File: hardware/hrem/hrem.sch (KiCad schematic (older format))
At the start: 27 parts, among them J1 AVR-ISP, J2 Hall_Conn, Q1 MMBT4401-7-F, SW1 SW_Push_Dual, U1 HT7733A, U2 ATtiny85, U3 74LVC1G125, U4 74LVC1G125

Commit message: Button footprint added
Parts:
- SW1: footprint Button_Switch_SMD:SW_Push_1P1T_NO_6x6mm_H9.5mm -> hrem:Diptronics DTSM-65N
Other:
- moved on the sheet: TP1
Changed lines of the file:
@@
-$EndComp
-$Comp
-L Device:Battery_Cell BT1
-U 1 1 5D9F4947
-P 1850 1900
-F 0 "BT1" H 1968 1996 50  0000 L CNN
-F 1 "1xAAA" H 1968 1905 50  0000 L CNN
-F 2 "hrem:AAA battery" V 1850 1960 50  0001 C CNN
-F 3 "~" V 1850 1960 50  0001 C CNN
-	1    1850 1900
-	1    0    0    -1
 $EndComp
 $Comp
@@
 	2600 1600 2700 1600
 Wire Wire Line
-	1850 2000 1850 2050
-Wire Wire Line
-	1850 2050 2200 2050
-Wire Wire Line
 	2600 2050 2600 2000
 Wire Wire Line
 	2200 2100 2200 2050
-Connection ~ 2200 2050
 Wire Wire Line
 	2200 2050 2600 2050
@@
 F 0 "SW1" V 7600 1348 50  0000 L CNN
 F 1 "SW_Push_Dual" V 7645 1348 50  0001 L CNN
-F 2 "Button_Switch_SMD:SW_Push_1P1T_NO_6x6mm_H9.5mm" H 7600 1400 50  0001 C CNN
+F 2 "hrem:Diptronics DTSM-65N" H 7600 1400 50  0001 C CNN
 F 3 "https://datasheet.lcsc.com/szlcsc/Diptronics-DTSM-65N-V-T-R_C224982.pdf" H 7600 1400 50  0001 C CNN
 F 4 "C224982" H 7600 1200 50  0001 C CNN "Part"
@@
 $EndComp
 $Comp
-L Connector:TestPoint_Flag TP1
-U 1 1 5E2E9580
-P 1950 2900
-F 0 "TP1" H 2210 2948 50  0000 L CNN
-F 1 "TestPoint_Flag" H 2210 2903 50  0001 L CNN
-F 2 "TestPoint:TestPoint_Loop_D2.50mm_Drill1.0mm" H 2150 2900 50  0001 C CNN
-F 3 "~" H 2150 2900 50  0001 C CNN
-	1    1950 2900
-	1    0    0    -1
-$EndComp
-$Comp
-L power:GND #PWR02
-U 1 1 5E2ED3E9
-P 1950 3000
-F 0 "#PWR02" H 1950 2750 50  0001 C CNN
-F 1 "GND" H 1955 2827 50  0000 C CNN
-F 2 "" H 1950 3000 50  0001 C CNN
-F 3 "" H 1950 3000 50  0001 C CNN
-	1    1950 3000
-	1    0    0    -1
-$EndComp
-Wire Wire Line
-	1950 2900 1950 3000
-$Comp
 L Connector:TestPoint_Flag TP2
 U 1 1 5E2F0DC2
@@
 Wire Wire Line
 	9400 4750 9400 4850
+Connection ~ 2200 2050
+Wire Wire Line
+	2050 2050 2200 2050
+Connection ~ 2050 2050
+$Comp
+L Connector:TestPoint_Flag TP1
+U 1 1 5E2E9580
+P 2050 2050
+F 0 "TP1" H 2300 2250 50  0000 R CNN
+F 1 "TestPoint_Flag" H 2310 2053 50  0001 L CNN
+F 2 "TestPoint:TestPoint_Loop_D2.50mm_Drill1.0mm" H 2250 2050 50  0001 C CNN
+F 3 "~" H 2250 2050 50  0001 C CNN
+	1    2050 2050
+	-1   0    0    1
+$EndComp
+Wire Wire Line
+	1850 2050 2050 2050
+Wire Wire Line
+	1850 2000 1850 2050
+$Comp
+L Device:Battery_Cell BT1
+U 1 1 5D9F4947
+P 1850 1900
+F 0 "BT1" H 1968 1996 50  0000 L CNN
+F 1 "1xAAA" H 1968 1905 50  0000 L CNN
+F 2 "hrem:AAA battery" V 1850 1960 50  0001 C CNN
+F 3 "~" V 1850 1960 50  0001 C CNN
+	1    1850 1900
+	1    0    0    -1
+$EndComp
 $EndSCHEMATC

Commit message: Work on PCB layout
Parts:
- J2: footprint Connector_JST:JST_EH_B3B-EH-A_1x03_P2.50mm_Vertical -> hrem:X8821WRS-03-9TSN; Part (none) -> C397433
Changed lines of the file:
@@
 F 0 "J2" V 8650 2600 50  0000 C CNN
 F 1 "Hall_Conn" V 8750 2600 50  0000 C CNN
-F 2 "Connector_JST:JST_EH_B3B-EH-A_1x03_P2.50mm_Vertical" H 8800 2600 50  0001 C CNN
-F 3 "~" H 8800 2600 50  0001 C CNN
+F 2 "hrem:X8821WRS-03-9TSN" H 8800 2600 50  0001 C CNN
+F 3 "https://datasheet.lcsc.com/szlcsc/1906141836_XKB-Enterprise-X8821WRS-03-9TSN_C397433.pdf" H 8800 2600 50  0001 C CNN
+F 4 "C397433" H 8800 2600 50  0001 C CNN "Part"
 	1    8800 2600
 	0    1    -1   0

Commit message: Replace 68R with 100R on LED for component unification purposes (15mA current)
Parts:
- R3: value 68R -> 100R; Part C204268 -> C193990
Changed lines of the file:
@@
 P 8950 1250
 F 0 "R3" V 9050 1250 50  0000 L CNN
-F 1 "68R" V 8850 1200 50  0000 L CNN
+F 1 "100R" V 8850 1200 50  0000 L CNN
 F 2 "Resistor_SMD:R_0805_2012Metric_Pad1.15x1.40mm_HandSolder" V 8880 1250 50  0001 C CNN
 F 3 "~" H 8950 1250 50  0001 C CNN
-F 4 "C204268" H 8950 1250 50  0001 C CNN "Part"
+F 4 "C193990" H 8950 1250 50  0001 C CNN "Part"
 	1    8950 1250
 	0    -1   -1   0

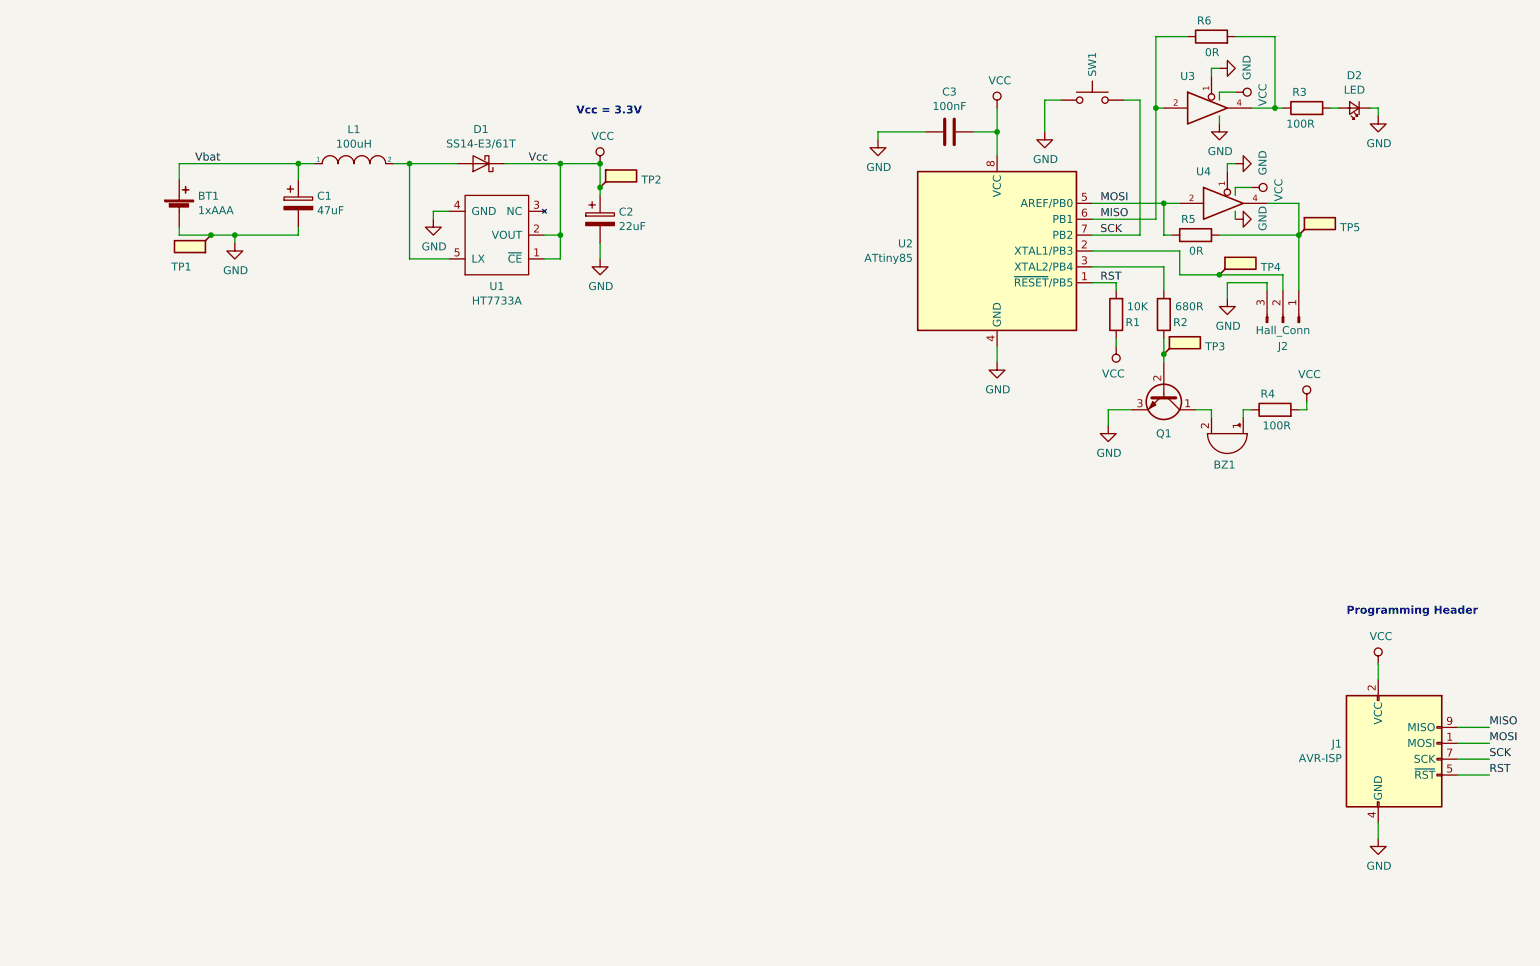
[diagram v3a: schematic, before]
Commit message: Decoupling caps added on U3 and U4
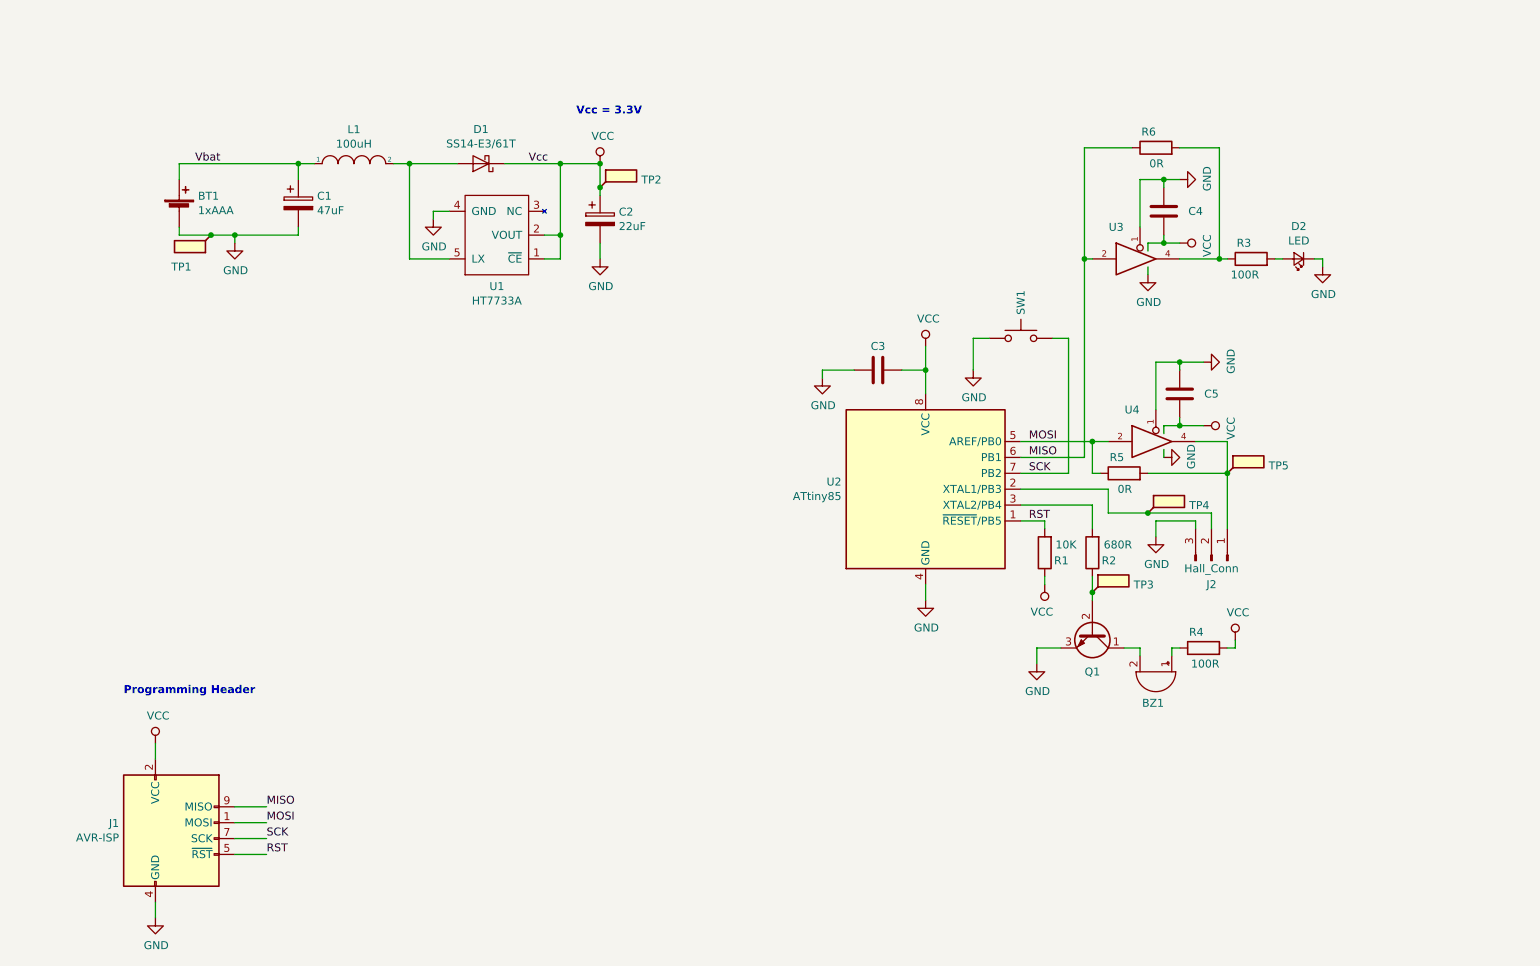
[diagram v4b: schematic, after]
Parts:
- added C4, C5: 100nF, Capacitor_SMD:C_0805_2012Metric_Pad1.15x1.40mm_HandSolder, symbol Device:C
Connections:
- net GND: now also C4.2, C5.2
- net VCC: now also C4.1, C5.1
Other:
- moved on the sheet: BZ1, C3, D2, J1, J2, Q1, R1, R2, R3, R4, R5, R6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

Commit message: Schematic cleanup
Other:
- note added: "Boost Controller\nVcc = 3.3V"
- note removed: "Vcc = 3.3V"
- moved on the sheet: BT1, C1, C2, C5, D1, J2, L1, R5, TP1, TP2, TP4, TP5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
